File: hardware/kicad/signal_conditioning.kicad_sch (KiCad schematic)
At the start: 0 parts

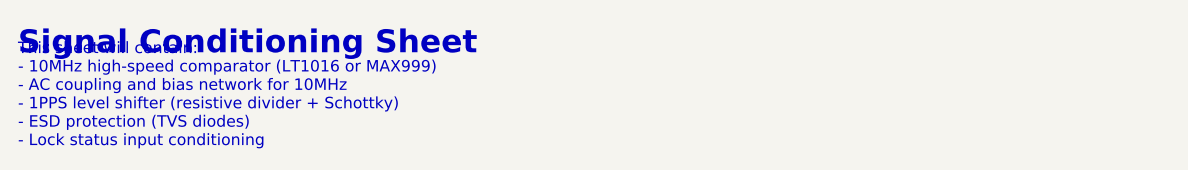
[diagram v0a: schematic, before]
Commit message: Update FE-5680A pinout and add NPN level shifter for lock detection
- Correct DB-9 pinout: Pin 1 (+15V), Pin 2 (GND), Pin 3 (Lock),
  Pin 4 (+5V), Pin 5 (GND), Pin 7 (10MHz)
- Add NPN transistor (2N3904) level shifter circuit for lock status:
  22k input resistor, 10k base-to-GND, 10k collector pull-up
- FE-5680A outputs 4.8V (unlocked) / 0.8V (locked)
- Transistor inverts signal: GPIO HIGH = locked, LOW = unlocked
- Update firmware to remove signal inversion in check_rb_lock()
- Remove internal pull-up (external pull-up via collector resistor)
- Update all documentation and schematics

🤖 Generated with [Claude Code](https://claude.com/claude-code)

Co-Authored-By: Claude Opus 4.5 <noreply@anthropic.com>
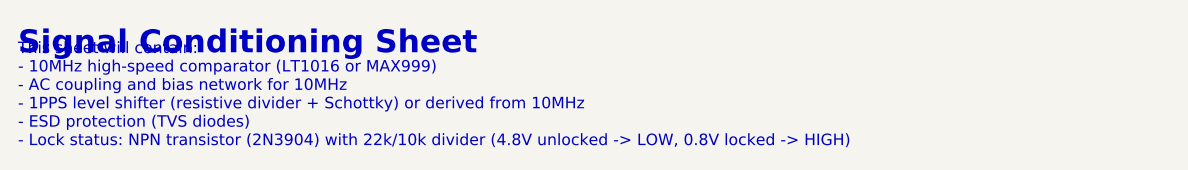
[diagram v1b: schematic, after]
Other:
- note added: "This sheet will contain: - 10MHz high-speed comparator (LT1016 or MAX999) - AC coupling and bias network for 10MHz - 1PPS level shifter (resistive divider + Schottky) or derived from 10MHz - ESD protection (TVS diodes) - Lock status: NPN transistor (2N3904) with 22k/10k divider (4.8V unlocked -> LOW, 0.8V locked -> HIGH)"
- note removed: "This sheet will contain: - 10MHz high-speed comparator (LT1016 or MAX999) - AC coupling and bias network for 10MHz - 1PPS level shifter (resistive divider + Schottky) - ESD protection (TVS diodes) - Lock status input conditioning"
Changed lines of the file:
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@@
 		(comment 1 "10MHz: 1Vpp sine -> 3.3V LVCMOS (LT1016/MAX999)")
 		(comment 2 "1PPS: 5V TTL -> 3.3V with ESD protection")
-		(comment 3 "Lock Status: Direct with current limiting")
+		(comment 3 "Lock Status: NPN level shifter (4.8V/0.8V -> 3.3V logic)")
 	)
 	(text "Signal Conditioning Sheet"
@@
 		)
 	)
-	(text "This sheet will contain:\n- 10MHz high-speed comparator (LT1016 or MAX999)\n- AC coupling and bias network for 10MHz\n- 1PPS level shifter (resistive divider + Schottky)\n- ESD protection (TVS diodes)\n- Lock status input conditioning"
+	(text "This sheet will contain:\n- 10MHz high-speed comparator (LT1016 or MAX999)\n- AC coupling and bias network for 10MHz\n- 1PPS level shifter (resistive divider + Schottky) or derived from 10MHz\n- ESD protection (TVS diodes)\n- Lock status: NPN transistor (2N3904) with 22k/10k divider (4.8V unlocked -> LOW, 0.8V locked -> HIGH)"
 		(exclude_from_sim no)
 		(at 50.8 60.96 0)
